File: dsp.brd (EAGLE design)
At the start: 190 x 113 mm, 128 parts, among them IC1 OPA2134P, IC2 OPA2134P, IC3 OPA2134P, U1 STM32F405RGT6, U2 CODECODER-WM8731SEDS/V(SSOP28), U4 LM2575HVS-3.3/NOPB, X1 ABLS-8.000MHZ-B4-T

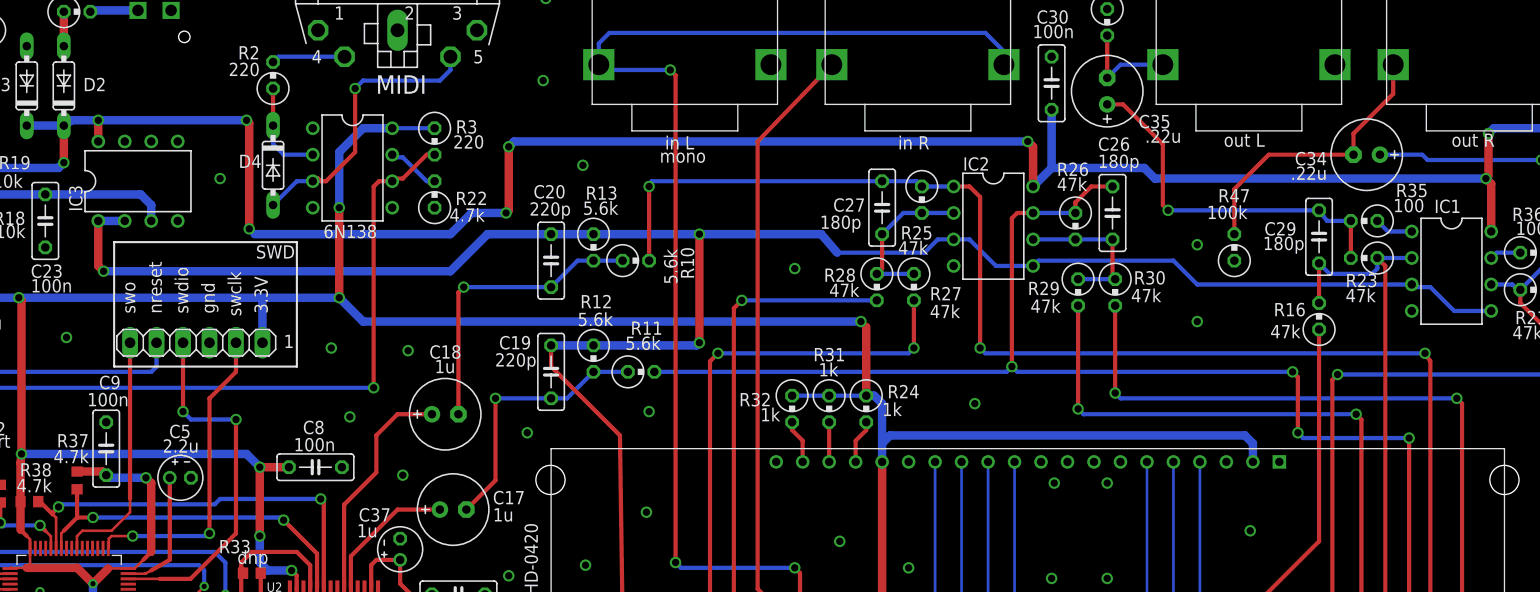
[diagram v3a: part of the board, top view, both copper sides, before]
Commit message: routing for mono on both inputs
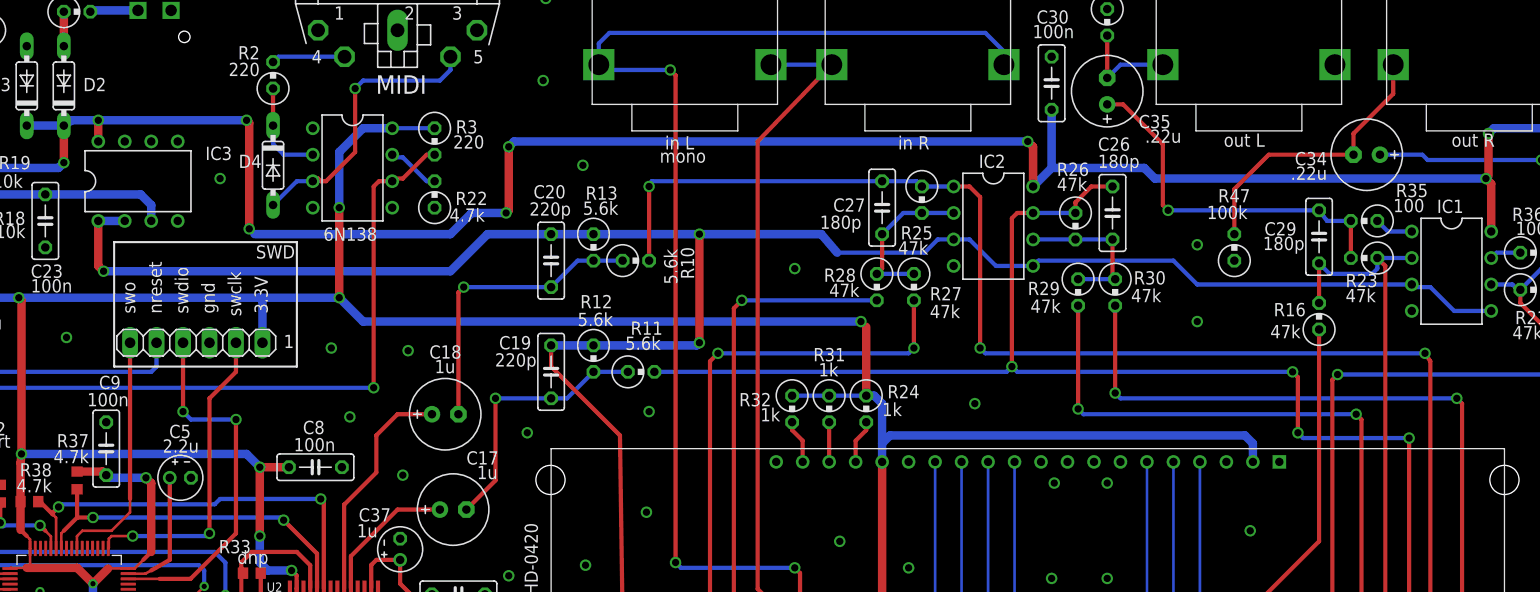
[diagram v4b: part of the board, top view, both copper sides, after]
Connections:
- net GND: no longer INL.P$1
- net N$29: now also INL.P$1
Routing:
- net N$29: track 84.2 -> 90.0 mm
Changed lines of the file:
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@@
 </element>
 <element name="C17" library="dan" package="E2,5-7" value="1u" x="72.39" y="53.086" smashed="yes">
-<attribute name="NAME" x="76.2" y="53.594" size="1.27" layer="21" font="vector" ratio="15"/>
-<attribute name="VALUE" x="76.2" y="51.943" size="1.27" layer="21" font="vector" ratio="15"/>
+<attribute name="NAME" x="73.66" y="57.404" size="1.27" layer="21" font="vector" ratio="15"/>
+<attribute name="VALUE" x="74.676" y="56.007" size="1.27" layer="21" font="vector" ratio="15"/>
 </element>
 <element name="C18" library="dan" package="E2,5-7" value="1u" x="71.628" y="62.23" smashed="yes">
@@
 </element>
 <element name="IC1" library="dan" package="DIL08" value="OPA2134P" x="168.148" y="75.946" smashed="yes" rot="R270">
-<attribute name="NAME" x="166.497" y="81.534" size="1.27" layer="21" font="vector" ratio="15"/>
+<attribute name="NAME" x="166.751" y="81.534" size="1.27" layer="21" font="vector" ratio="15"/>
 </element>
 <element name="IC2" library="dan" package="DIL08" value="OPA2134P" x="124.206" y="80.264" smashed="yes" rot="R270">
-<attribute name="NAME" x="121.285" y="85.598" size="1.27" layer="21" font="vector" ratio="15"/>
+<attribute name="NAME" x="122.809" y="85.852" size="1.27" layer="21" font="vector" ratio="15"/>
 </element>
 <element name="J1" library="dan" package="SPC4077" value="" x="15.748" y="101.092" smashed="yes" rot="R270">
@@
 <attribute name="MF" value="VISHAY/TELEFUNKEN" x="62.738" y="85.852" size="1.778" layer="27" rot="R270" display="off"/>
 <attribute name="OC_FARNELL" value="9860150" x="62.738" y="85.852" size="1.778" layer="27" rot="R270" display="off"/>
-<attribute name="VALUE" x="59.944" y="79.121" size="1.27" layer="21" font="vector" ratio="15"/>
+<attribute name="VALUE" x="59.944" y="78.867" size="1.27" layer="21" font="vector" ratio="15"/>
 </element>
 <element name="R2" library="dan" package="0309V" value="220" x="55.118" y="94.742" smashed="yes" rot="R90">
@@
 </element>
 <element name="IC3" library="dan" package="DIL08" value="OPA2134P" x="42.164" y="84.582" smashed="yes">
-<attribute name="NAME" x="36.83" y="81.661" size="1.27" layer="21" font="vector" ratio="15" rot="R90"/>
+<attribute name="NAME" x="51.181" y="87.884" size="1.27" layer="21" font="vector" ratio="15" rot="R180"/>
 </element>
 <element name="C23" library="dan" package="C050-025X075" value="100n" x="33.274" y="80.772" smashed="yes" rot="R270">
@@
 <contactref element="IC2" pad="4"/>
 <contactref element="INL" pad="P$3"/>
-<contactref element="INL" pad="P$1"/>
 <contactref element="INL" pad="P$2"/>
 <contactref element="INR" pad="P$2"/>
@@
 <wire x1="101.6" y1="45.466" x2="101.6" y2="88.392" width="0.4064" layer="1"/>
 <wire x1="101.6" y1="88.392" x2="108.712" y2="95.758" width="0.4064" layer="1"/>
+<contactref element="INL" pad="P$1"/>
+<wire x1="102.87" y1="95.758" x2="108.712" y2="95.758" width="0.4064" layer="16"/>
 </signal>
 <signal name="N$31">

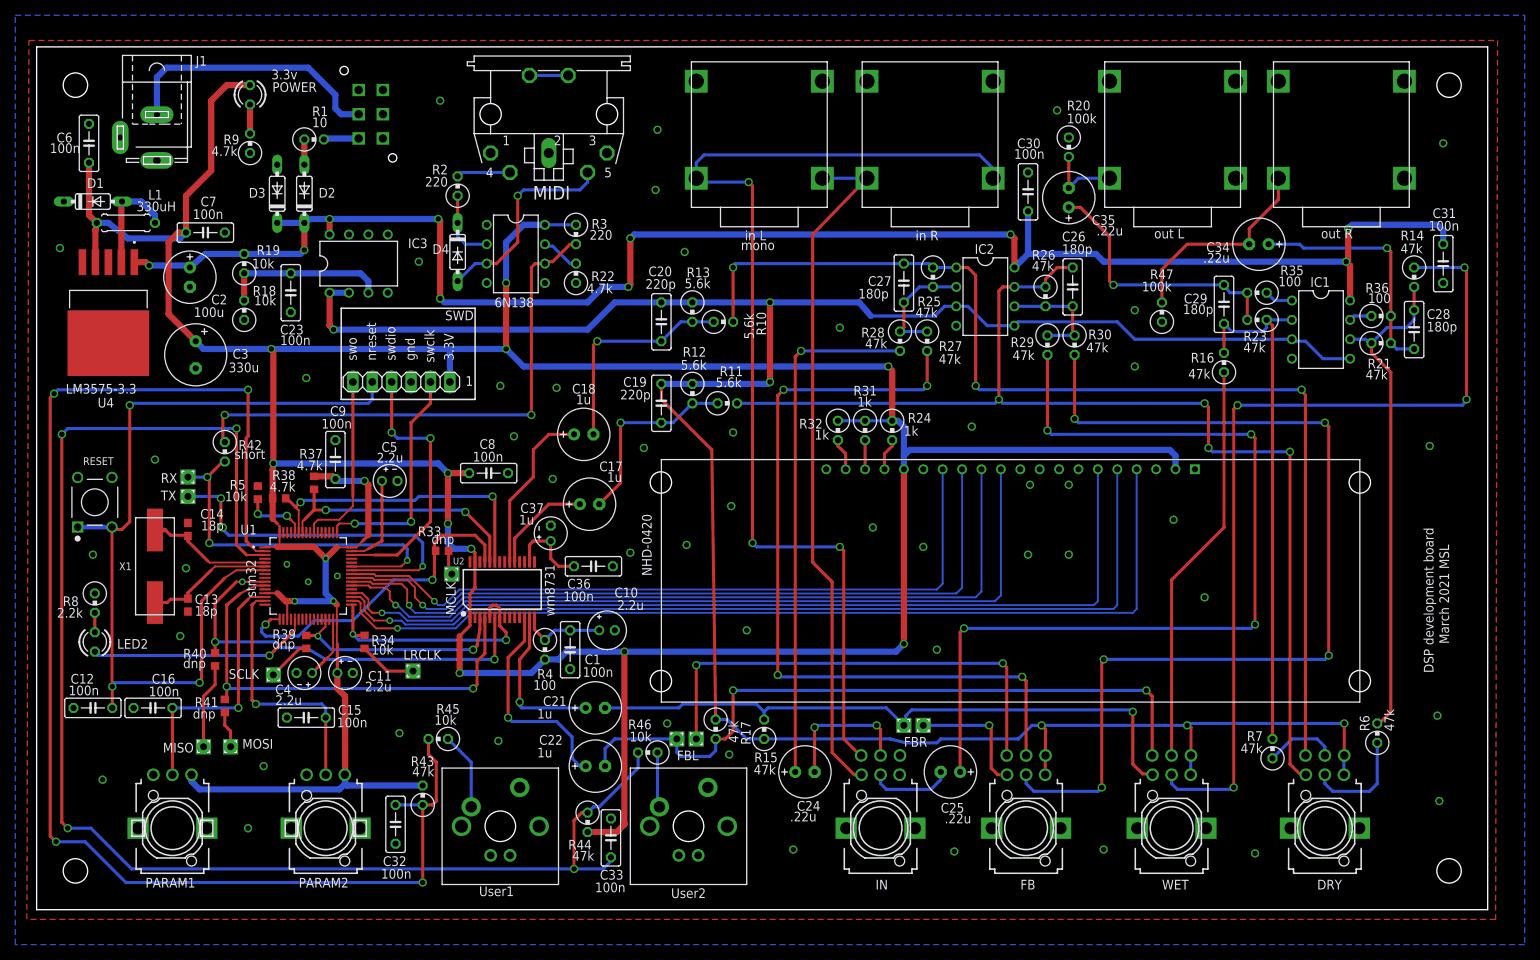
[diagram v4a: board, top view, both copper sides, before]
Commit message: connected mode and csb on wm8731
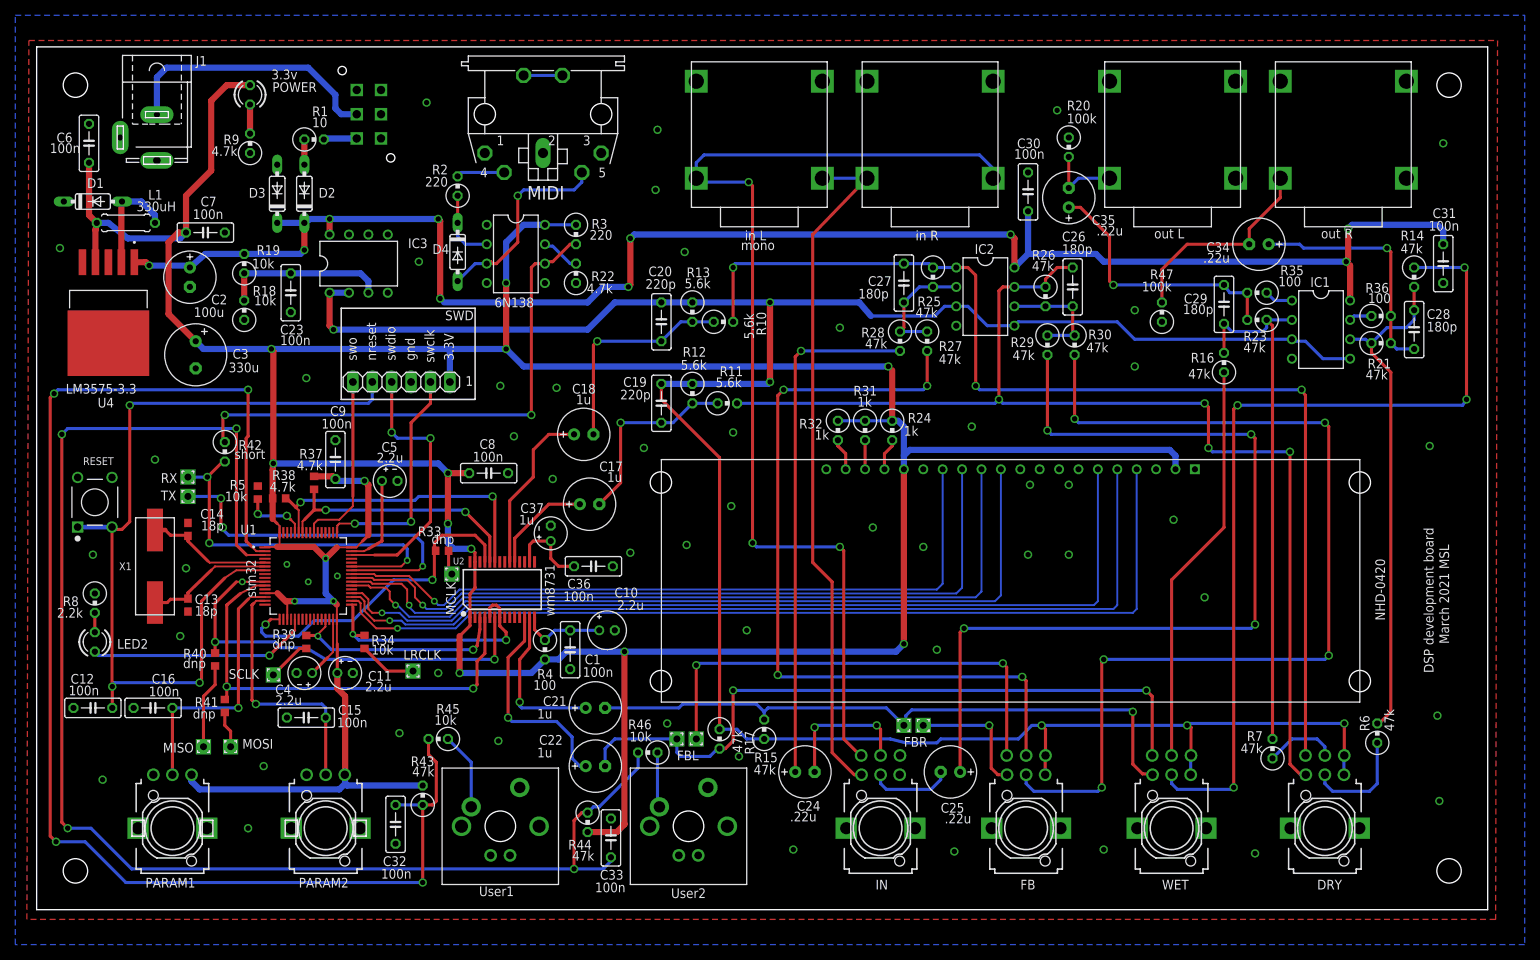
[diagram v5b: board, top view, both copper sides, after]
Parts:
- moved R17 1.37 mm to (89.4, 22.4)
- moved MIDI 0.76 mm to (66.3, 104.1)
- moved OUTR 0.25 mm to (179.3, 95.8)
- moved U$2 0.25 mm to (43.2, 104.1)
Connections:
- net GND: now also U2.21, U2.22
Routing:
- net N$41: track 27.4 -> 26.7 mm
- net N$40: track 7.07 -> 6.31 mm
- net 4.5V: track 322.9 -> 323.5 mm

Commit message: added a ground for vccref and moved icp header to edge
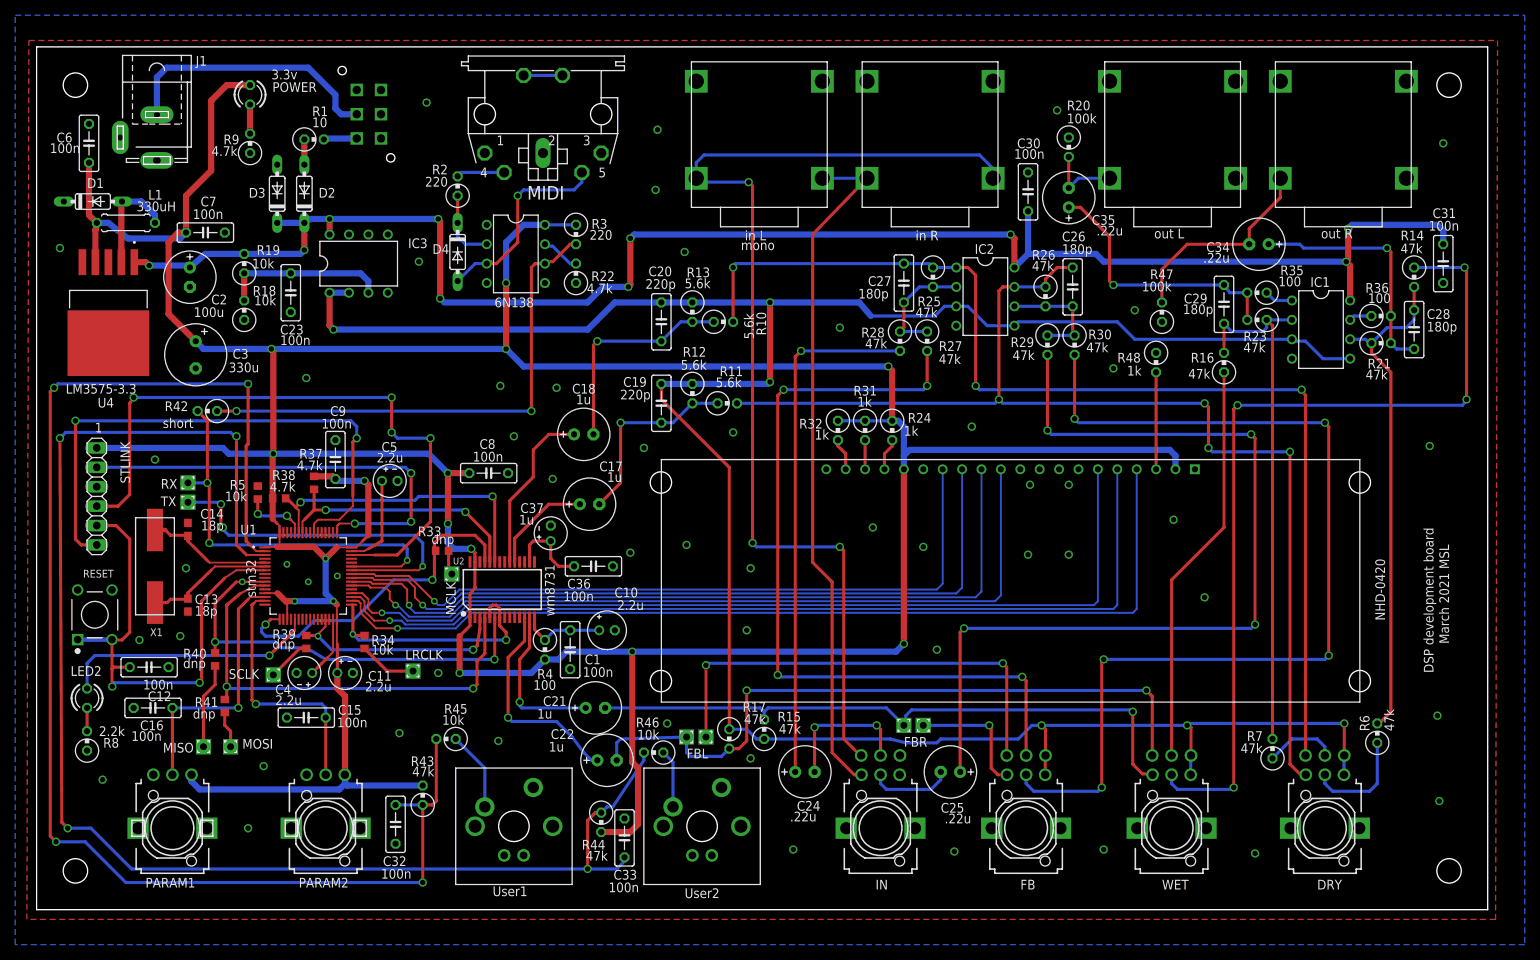
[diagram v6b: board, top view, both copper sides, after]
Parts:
- removed SWD: (no value), dan:1X06
- added R48: 1k, dan:0309V
- added STLINK: (no value), dan:1X06
- moved R8 18.1 mm to (6.60, 22.1), turned to 90 degrees
- moved RESET 14.7 mm to (7.62, 38.6)
- moved C12 9.09 mm to (14.7, 31.8), turned to 180 degrees
- moved LED2 7.44 mm to (6.60, 27.7), turned to 270 degrees
- moved R42 5.80 mm to (22.4, 65.3), turned to 180 degrees
- moved C33 1.78 mm to (77.0, 9.40)
- moved R44 1.78 mm to (73.9, 11.4)
- moved U$4 1.78 mm to (87.1, 10.9)
- moved U$3 1.78 mm to (62.5, 10.9)
- moved C22 1.70 mm to (74.7, 19.6)
- moved FBL 1.30 mm to (85.1, 22.6)
- moved FBL1 1.30 mm to (87.6, 22.6)
- moved R17 1.27 mm to (90.7, 22.4)
- moved R45 1.02 mm to (53.6, 22.4)
- moved R46 0.76 mm to (80.8, 20.6)
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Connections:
- new net N$59: R48.2, U$1.P$3
- net 3.3V: now also STLINK.1; no longer SWD.1
- net GND: now also R48.1, STLINK.3; no longer SWD.3
- net NRESET: now also STLINK.5; no longer SWD.5
- net SWCLK: now also STLINK.2; no longer SWD.2
- net SWDIO: now also STLINK.4; no longer SWD.4
- net SWO: now also STLINK.6; no longer SWD.6
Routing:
- net SWO: track 23.5 -> 73.6 mm, vias 0 -> 2
- net SWDIO: track 35.1 -> 84.6 mm, vias 2 -> 4
- net NRESET: track 113.1 -> 65.5 mm, vias 3 -> 2
- net SWCLK: track 30.2 -> 58.6 mm, vias 2 -> 3
- net 3.3V: track 545.0 -> 564.8 mm
- net N$59: track 0.00 -> 12.7 mm
- net N$50: track 49.8 -> 55.8 mm
- net N$9: track 29.2 -> 33.7 mm
- net MIDIIN: track 70.3 -> 67.0 mm
- net FBL: track 91.9 -> 90.4 mm
- net N$55: track 62.2 -> 60.6 mm
- net SWITCH1: track 182.2 -> 183.3 mm
- net N$8: track 48.1 -> 47.3 mm
- net 4.5V: track 323.5 -> 322.8 mm
- net N$10: track 2.54 -> 3.05 mm
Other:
- board text removed: "3.3V"
- board text removed: "gnd"
- board text removed: "nreset"
- board text removed: "swclk"
- board text removed: "swdio"
- board text removed: "swo"

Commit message: added a mclk optin for pc6 for f405 compatibility
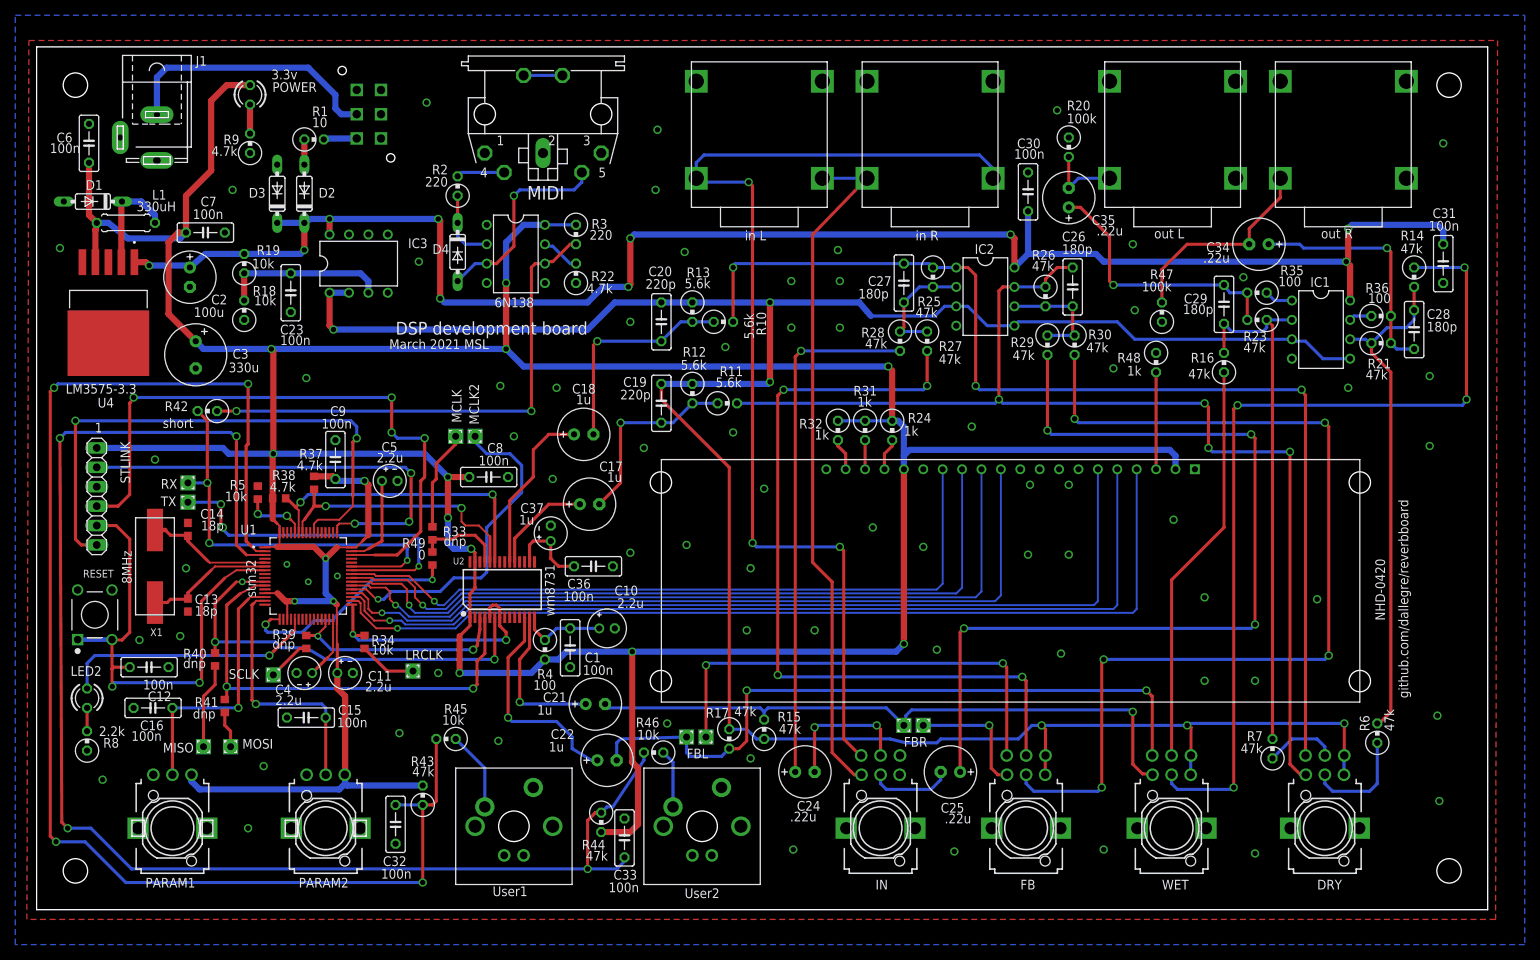
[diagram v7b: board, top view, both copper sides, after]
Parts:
- added MCLK2: (no value), synthdiy:2,0/0,9-S
- added R49: 0, dan:R0603
- moved MCLK 18.0 mm to (54.9, 62.0), turned to 90 degrees
- moved R33 2.62 mm to (51.8, 49.3), turned to 90 degrees
- moved C21 0.51 mm to (73.2, 26.9)
- moved C8 0.51 mm to (59.2, 56.6)
- moved C1 0.25 mm to (69.8, 34.3)
- moved C10 0.25 mm to (74.7, 36.8)
- turned D1 to 180 degrees
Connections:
- new net MCLK2: MCLK2.1, U1.37
- new net N$25: R49.1, U1.17
- net GND: now also D1.A; no longer D1.C
- net MCLK: now also R49.2; no longer U1.17
- net N$4: now also D1.C; no longer D1.A
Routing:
- net MCLK2: track 0.00 -> 43.7 mm, vias 0 -> 1
- net MCLK: track 44.2 -> 11.5 mm, vias 2 -> 0
- net N$25: track 0.00 -> 29.8 mm, vias 0 -> 2
- net N$45: track 3.22 -> 13.1 mm
- net SCL: track 34.1 -> 35.2 mm
- net SWDIO: track 84.6 -> 83.5 mm
- net N$8: track 47.3 -> 46.6 mm
- net LOUT: track 28.2 -> 28.7 mm
- net ROUT: track 20.8 -> 20.3 mm
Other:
- board text added: "8MHz"
- board text added: "github.com/dallegre/reverbboard"
- board text removed: "mono"
